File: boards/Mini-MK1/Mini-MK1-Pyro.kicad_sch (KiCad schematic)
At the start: 36 parts, among them U1 TCAL9538-UQFN, U2 TPS3842-Q1, U3 MAX14575CETA+

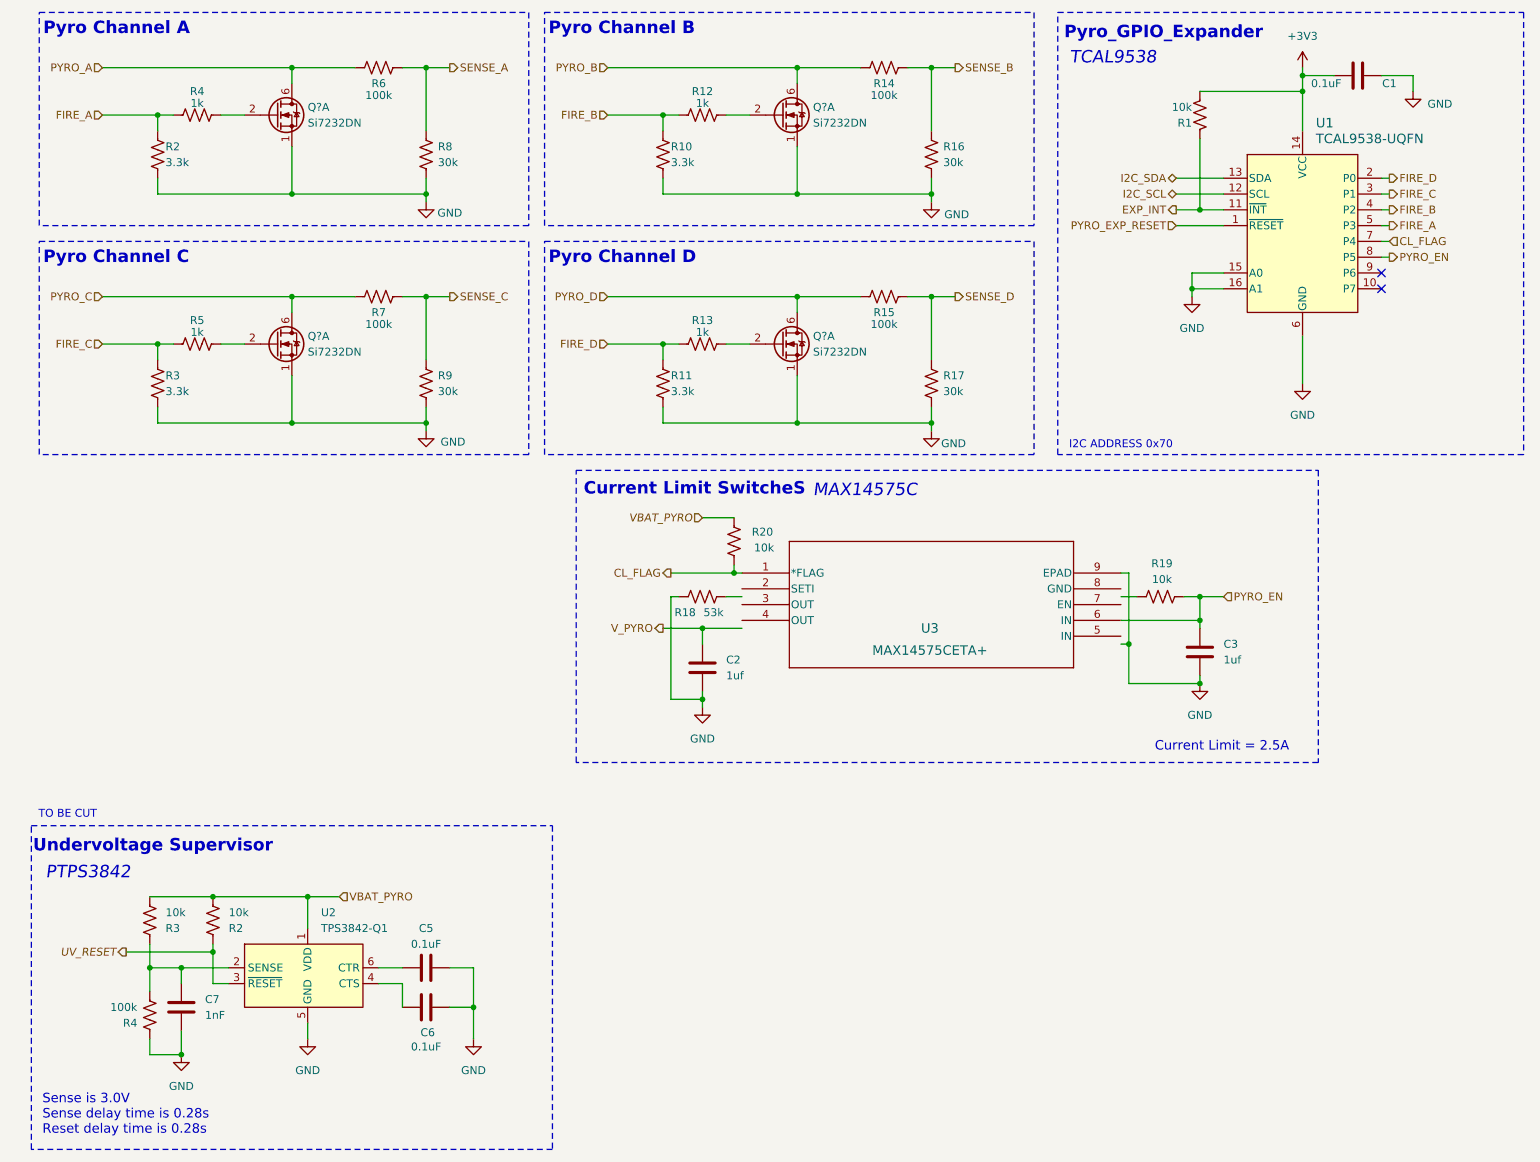
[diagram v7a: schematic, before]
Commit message: Edited MAX board and pin names, added contributors' names, deleted undervoltage supervisor
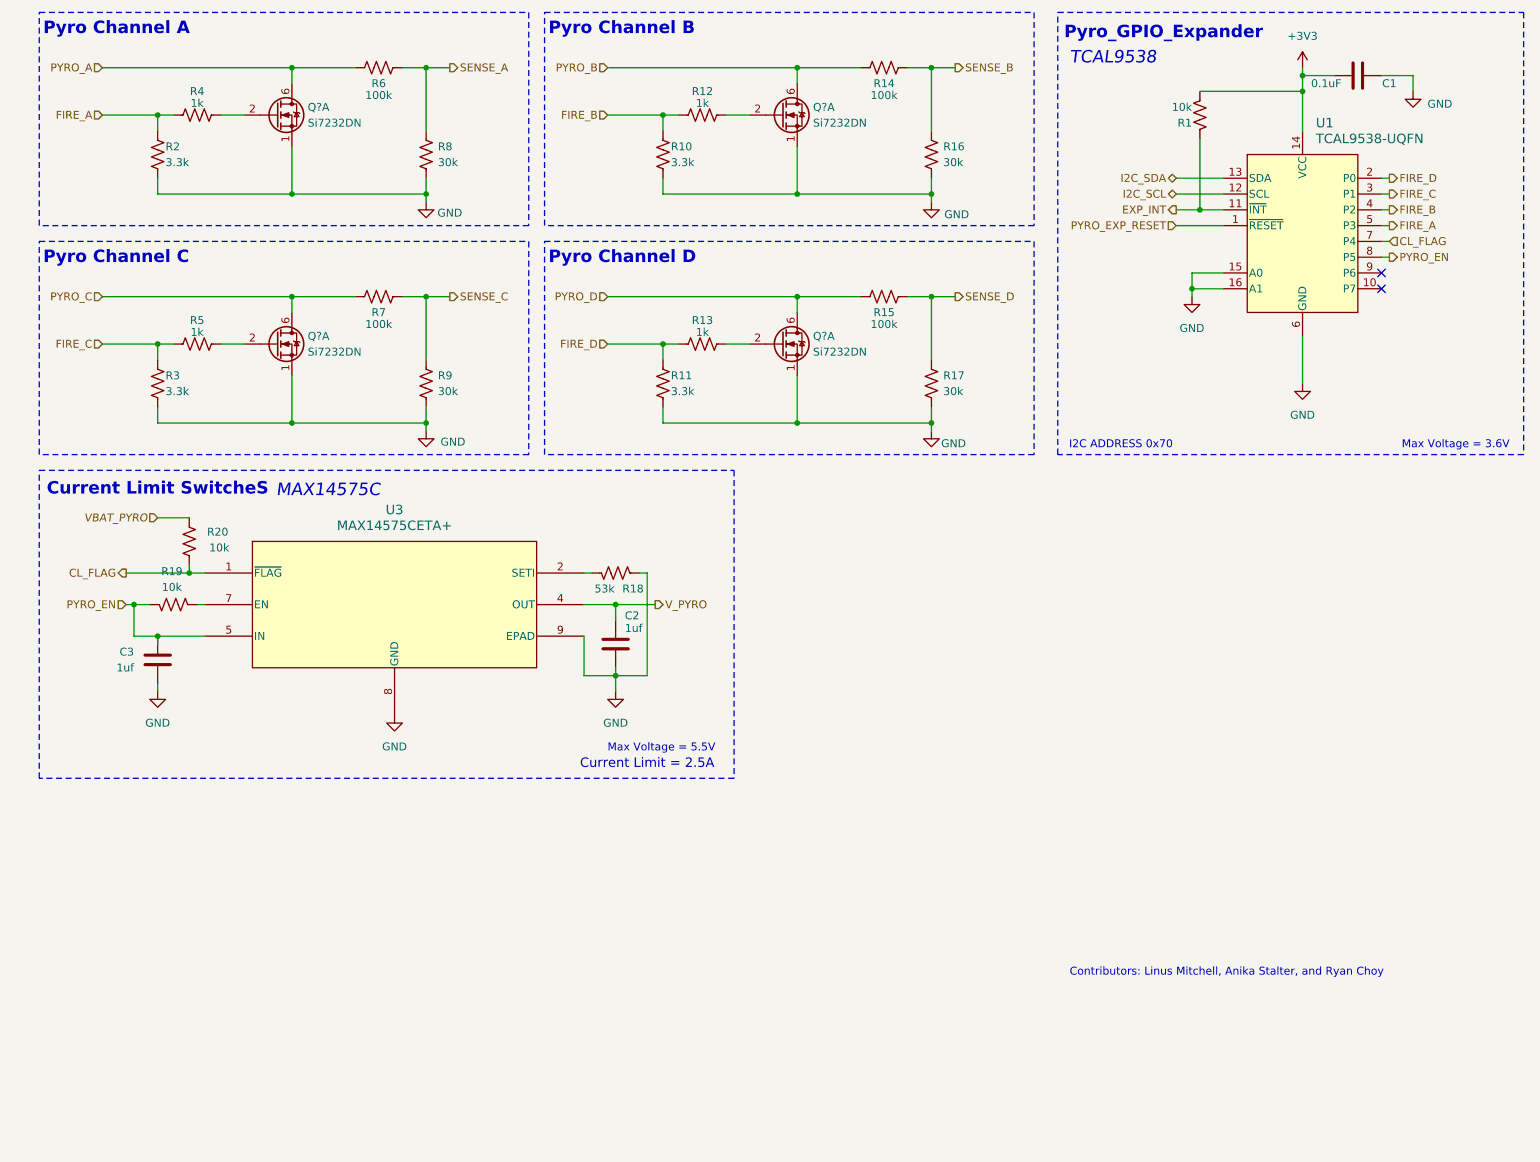
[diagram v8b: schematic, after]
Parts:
- removed 100k: R4, symbol Device:R_US
- removed 10k: R2, symbol Device:R_US
- removed 10k: R3, symbol Device:R_US
- removed C5, C6: 0.1uF, symbol Device:C
- removed C7: 1nF, symbol Device:C
- removed U2: TPS3842-Q1, Package_TO_SOT_SMD:Texas_R-PDSO-N6_DRL-6, symbol Power_Supervisor_Texas:TPS3842-Q1
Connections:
- net GND: now also U3.8 (GND)
- net PYRO_EN: now also U3.5 (IN)
- net V_PYRO: now also U3.3 (OUT), U3.4 (OUT)
- net at R18.2: now also U3.2 (SETI)
- net at U3.7 (EN): now also R19.1
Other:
- note added: "Contributors: Linus Mitchell, Anika Stalter, and Ryan Choy"
- note added: "Max Voltage = 3.6V"
- note added: "Max Voltage = 5.5V"
- note removed: "PTPS3842"
- note removed: "Sense is 3.0V Sense delay time is 0.28s Reset delay time is 0.28s"
- note removed: "TO BE CUT"
- note removed: "Undervoltage Supervisor"
- moved on the sheet: C2, C3, R18, R19, R20
